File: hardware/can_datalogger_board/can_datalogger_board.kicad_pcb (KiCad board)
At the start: 2 copper layers, 90 x 110 mm, 107 parts, among them J1 AMP_Superseal_9-6437287-8, Q1 BSS138, Q2 BSS138, Q3 BSS138, Q4 BSS138, Q5 BSS138, SW1 JS202011SCQN, SW2 JS202011SCQN, U1 RASPBERRY_PI_ZERO_2_W, U10 SLG55021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

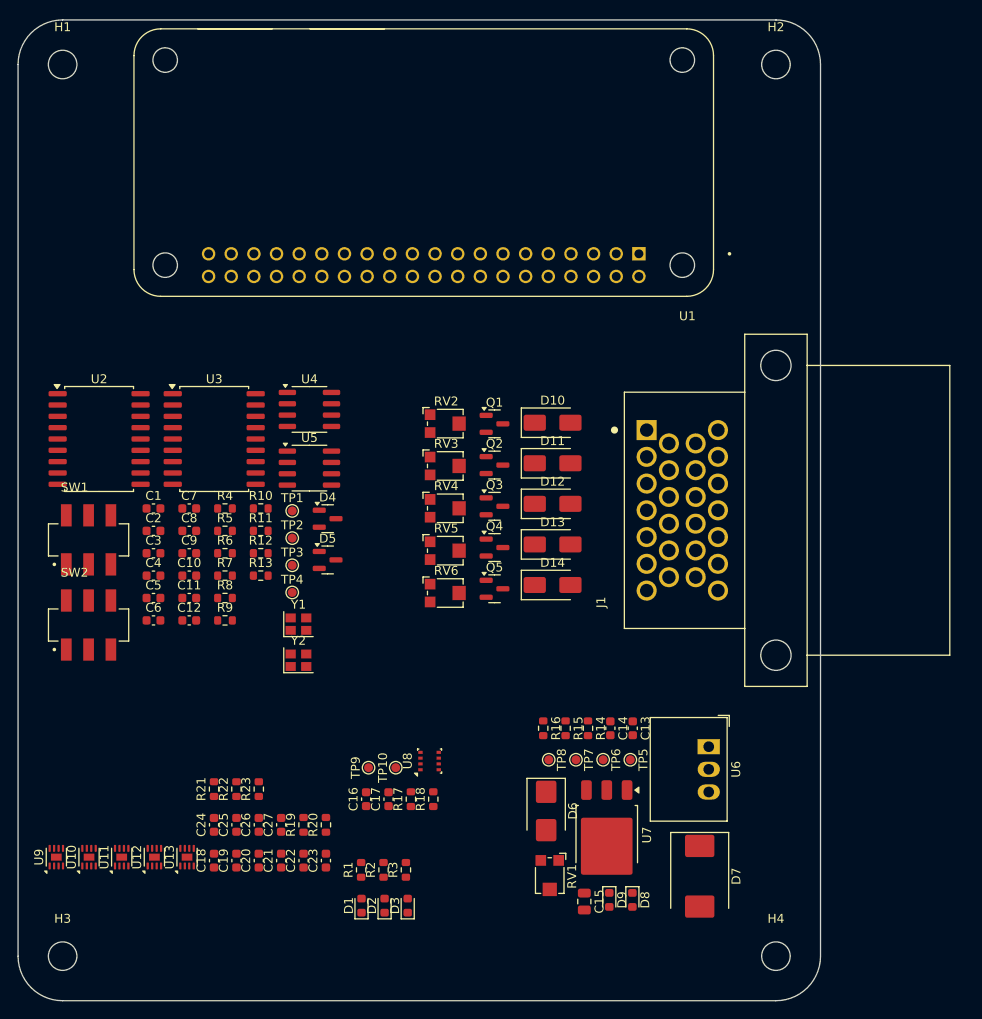
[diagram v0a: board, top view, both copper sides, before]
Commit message: PCB component placement
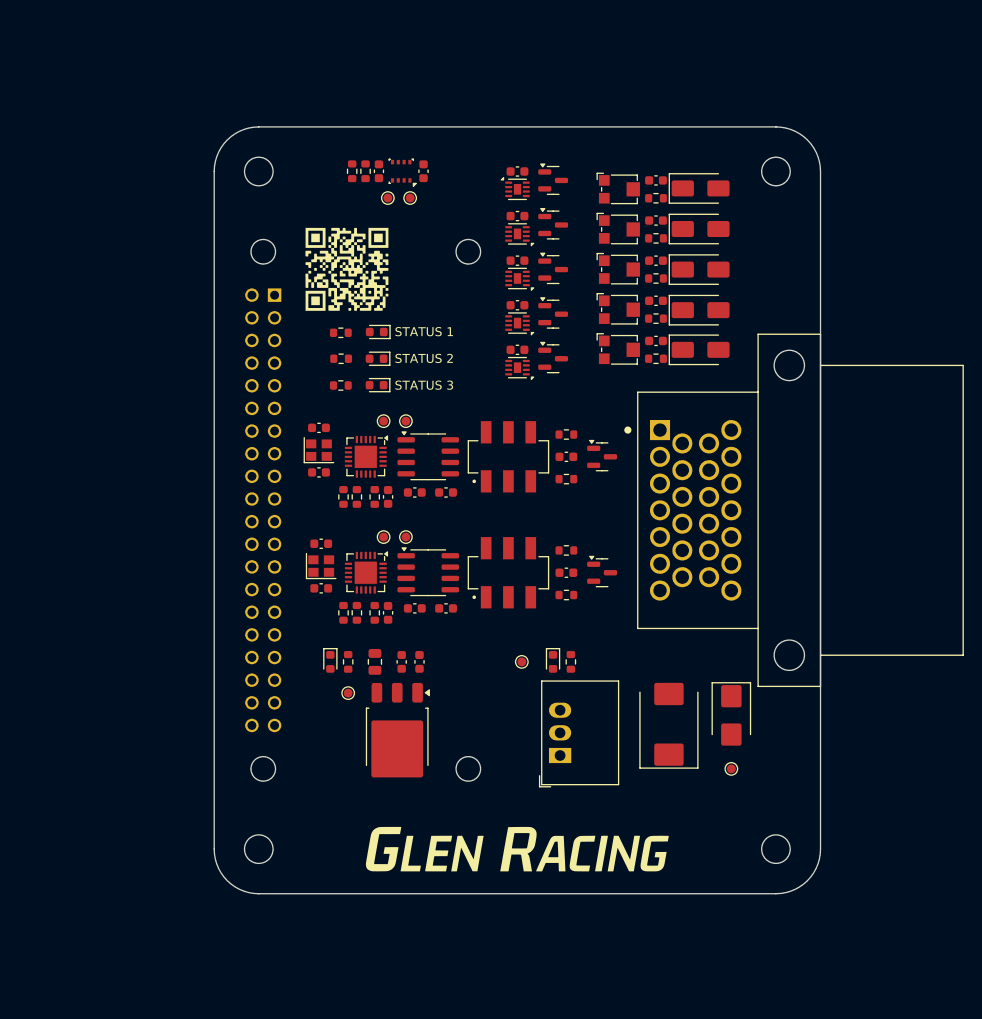
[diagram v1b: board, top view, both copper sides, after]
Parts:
- removed R14: 2.2k, Resistor_SMD:R_0603_1608Metric
- removed RV1: 10k Trim Pot, Potentiometer_SMD:Potentiometer_Bourns_TC33X_Vertical
- removed TP5: BATT_MEAS, TestPoint:TestPoint_Pad_D1.0mm
- added G***: LOGO, can_datalogger_board:glen_racing_logo, F.Cu at (161.0, 138.0)
- added G***: LOGO, can_datalogger_board:repo_link, F.Cu at (142.0, 73.0)
- U1: moved to B.Cu
- U2, U3: footprint Package_SO:SOIC-18W_7.5x11.6mm_P1.27mm -> Package_DFN_QFN:QFN-20-1EP_4x4mm_P0.5mm_EP2.5x2.5mm
- moved C20 88.3 mm to (176.6, 63.0), turned to 180 degrees
- moved U13 83.6 mm to (161.0, 64.0), turned to 0 degrees
- moved C21 83.2 mm to (176.6, 67.5), turned to 180 degrees
- moved U12 80.9 mm to (161.0, 69.0), turned to 180 degrees
- moved R19 80.6 mm to (176.6, 65.0), turned to 180 degrees
- moved U11 78.6 mm to (161.0, 74.0), turned to 180 degrees
- moved C22 78.0 mm to (176.6, 72.0), turned to 180 degrees
- moved C27 77.9 mm to (161.0, 62.0), turned to 180 degrees
- moved U10 76.8 mm to (161.0, 79.0), turned to 180 degrees
- moved R21 75.7 mm to (176.6, 74.0), turned to 180 degrees
- moved R20 75.5 mm to (176.6, 69.5), turned to 180 degrees
- moved U9 75.4 mm to (161.0, 84.0), turned to 180 degrees
- moved C25 75.2 mm to (161.0, 67.0), turned to 180 degrees
- moved C23 72.9 mm to (176.6, 76.5), turned to 180 degrees
- moved C24 71.8 mm to (161.0, 72.0), turned to 180 degrees
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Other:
- board size 90 x 110 mm -> 68 x 86 mm
- board text added: "STATUS 1"
- board text added: "STATUS 2"
- board text added: "STATUS 3"
